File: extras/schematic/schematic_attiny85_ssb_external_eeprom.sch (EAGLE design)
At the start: 27 parts, among them U1 SI4735-D60-GU, U2 328P, Y2 12MHz

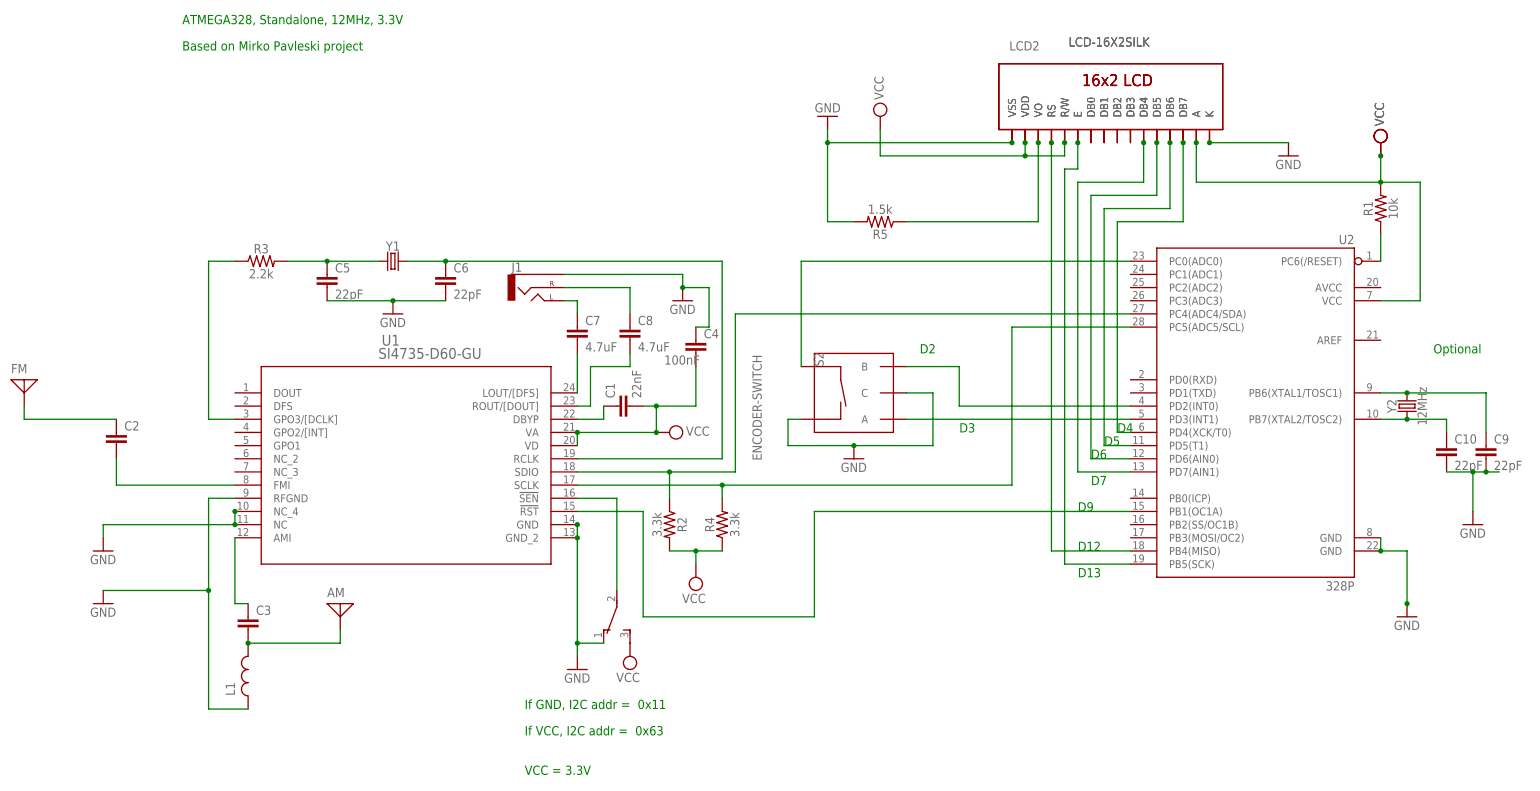
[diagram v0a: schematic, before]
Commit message: SI473X Arduino Library
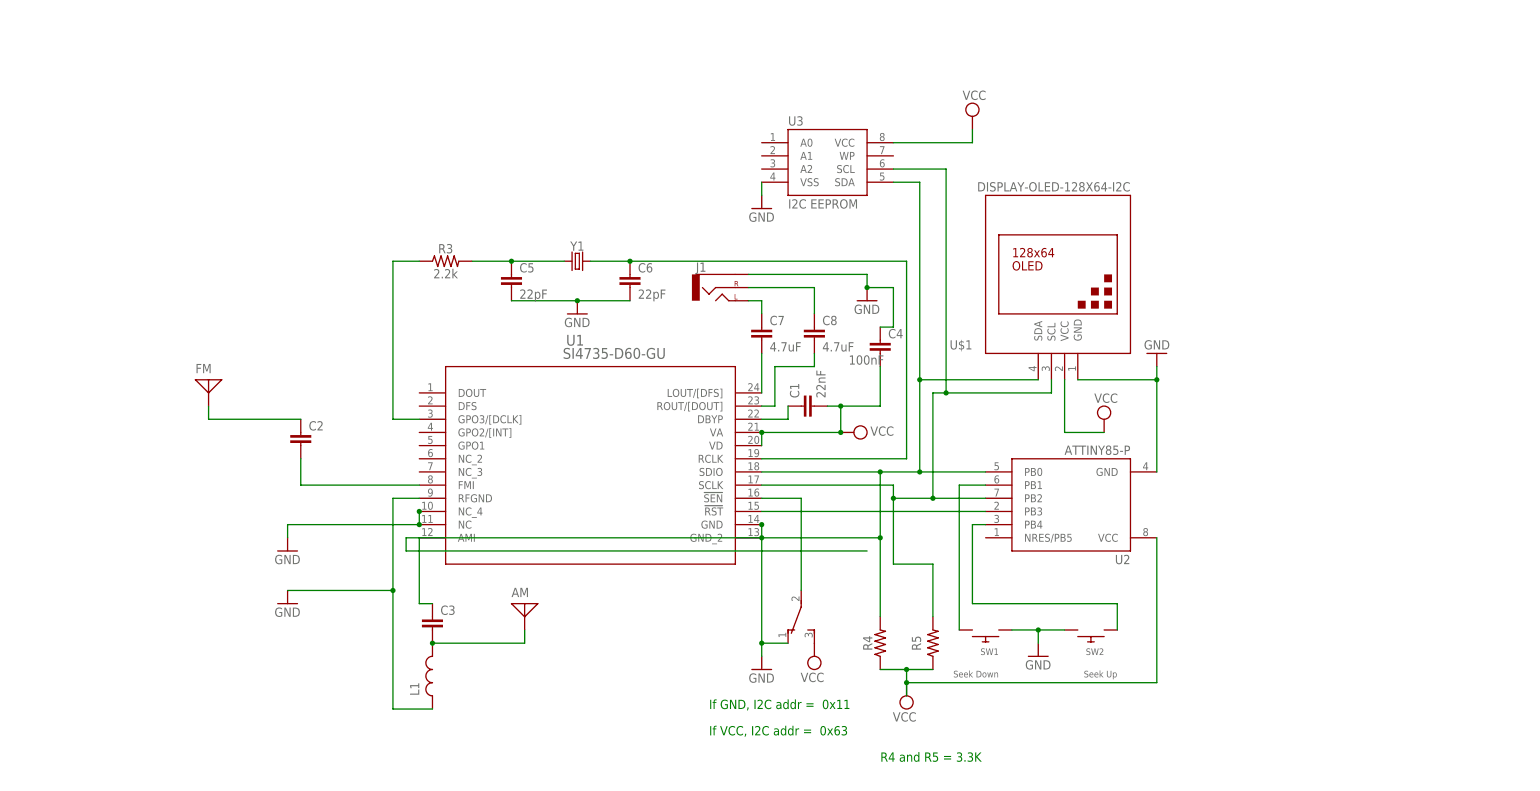
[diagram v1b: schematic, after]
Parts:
- removed C10, C9: 22pF, SparkFun-Capacitors:22PF-0603-50V-5%
- removed LCD1, LCD2: LCD-16X2SILK, SparkFun-Displays:LCD-16X2SILK
- removed R1: 10k, SparkFun-Resistors:10KOHM-0603-1/10W-1%
- removed R2: 3.3k, SparkFun-Resistors:3.3KOHM-0603-1/10W-1%
- removed S2: ENCODER-SWITCH, SparkFun-Switches:ENCODER-SWITCH
- removed Y2: 12MHz, SparkFun-Clocks:CRYSTAL-12MHZ"
- added SW1: Seek Down, adafruit:SWITCH_PUSHBUTTONEVQ-PE
- added SW2: Seek Up, adafruit:SWITCH_PUSHBUTTONEVQ-PE
- added U$1: DISPLAY-OLED-128X64-I2C, diy-modules:DISPLAY-OLED-128X64-I2C
- added U3: I2C EEPROM, SparkFun-IC-Memory:EEPROM-I2CEIAJ
- R4: value 3.3k -> 4.7k; device SparkFun-Resistors:3.3KOHM-0603-1/10W-1% -> SparkFun-Resistors:4.7KOHM-0603-1/10W-1%
- R5: value 1.5k -> 4.7k; device SparkFun-Resistors:1.5KOHM-0603-1/10W-1% -> SparkFun-Resistors:4.7KOHM-0603-1/10W-1%
- U2: value 328P -> ATTINY85-P; device SparkFun-IC-Microcontroller:ATMEGA328P_PDIP -> _hhn_attiny25_45_85:ATTINY85-P
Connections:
- removed net N$18: R2.1, U1.SDIO, U2.PC4(ADC4/SDA)
- removed net N$19: LCD1.DB7, LCD2.DB7, U2.PD4(XCK/T0)
- removed net N$20: U1.!RST, U2.PB1(OC1A)
- removed net N$21: LCD1.DB6, LCD2.DB6, U2.PD5(T1)
- removed net N$22: LCD1.DB5, LCD2.DB5, U2.PD6(AIN0)
- removed net N$23: LCD1.DB4, LCD2.DB4, U2.PD7(AIN1)
- removed net N$24: S2.B, U2.PD2(INT0)
- removed net N$25: LCD1.DB0, LCD2.DB0
- removed net N$26: LCD1.DB1, LCD2.DB1
- removed net N$27: LCD1.DB2, LCD2.DB2
- removed net N$28: LCD1.DB3, LCD2.DB3
- removed net N$29: LCD1.E, LCD2.E, U2.PB5(SCK)
- removed net N$31: S2.SW+, U2.PC0(ADC0)
- removed net N$32: LCD1.RS, LCD2.RS, U2.PB4(MISO)
- removed net N$33: S2.A, U2.PD3(INT1)
- removed net N$34: LCD1.VO, LCD2.VO, R5.1
- new net SDA: R5.2, U$1.SCL, U1.SCLK, U2.PB2, U3.SCL
- net GND: now also SW1.P$1, SW2.P$2, U$1.GND, U2.GND, U3.VSS; no longer C10.2, C9.2, LCD1.K, LCD1.VSS, LCD2.K, LCD2.VSS, R5.2, S2.C, S2.SW-, U2.GND@1, U2.GND@2
- net N$1: now also U1.!RST, U2.PB3; no longer R1.1, U2.PC6(/RESET)
- net N$15: now also U$1.SDA, U1.SDIO, U2.PB0, U3.SDA; no longer U1.SCLK, U2.PC5(ADC5/SCL)
- net N$16: now also SW1.P$2, U2.PB1; no longer C9.1, U2.PB6(XTAL1/TOSC1), Y2.2
- net N$17: now also SW2.P$1, U2.PB4; no longer C10.1, U2.PB7(XTAL2/TOSC2), Y2.1
- net VCC: now also R5.1, U$1.VCC, U3.VCC; no longer LCD1.A, LCD1.R/W, LCD1.VDD, LCD2.A, LCD2.R/W, LCD2.VDD, R1.2, R2.2
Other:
- note added: "R4 and R5 = 3.3K"
- note removed: "ATMEGA328, Standalone, 12MHz, 3.3V"
- note removed: "Based on Mirko Pavleski project"
- note removed: "D12"
- note removed: "D13"
- note removed: "D2"
- note removed: "D3"
- note removed: "D4"
- note removed: "D5"
- note removed: "D6"
- note removed: "D7"
- note removed: "D9"
- note removed: "VCC = 3.3V"
- moved on the sheet: AM, C1, C2, C3, C4, C5, C6, C7, C8, FM, J1, L1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
